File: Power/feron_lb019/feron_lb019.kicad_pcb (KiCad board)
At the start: 2 copper layers, 198 x 53 mm, 51 parts, among them J1 Conn_4pin01, J2 Conn_3pin01, P1 PC817, T1 TF8N60, U2 TL431, U3 OB2268

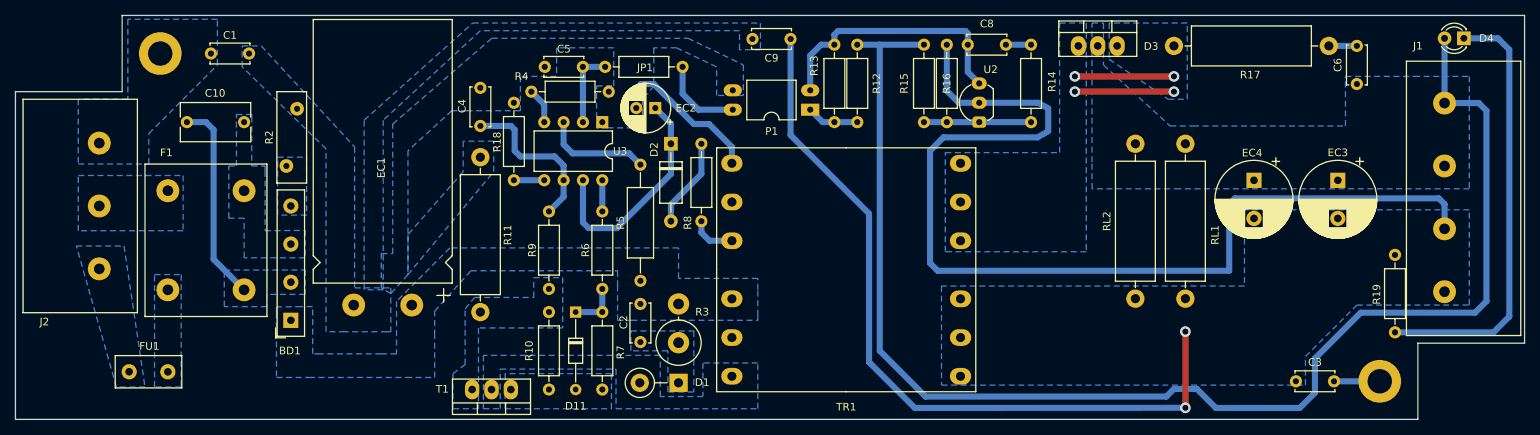
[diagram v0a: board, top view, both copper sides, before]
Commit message: R6. +24V, R1
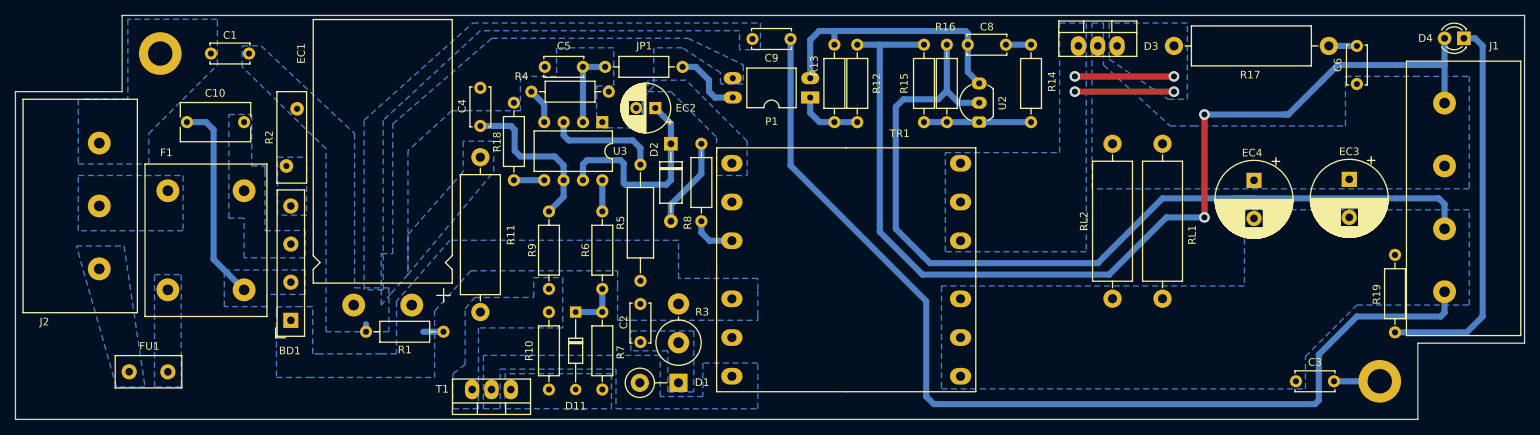
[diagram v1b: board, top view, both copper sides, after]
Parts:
- added R1: 510k, Resistor_THT:R_Axial_DIN0207_L6.3mm_D2.5mm_P10.16mm_Horizontal, F.Cu at (92.2, 111.5)
- RL1, RL2: value 1k -> 2k
- TR1: value Transformer_Feron1 -> PQ3220
- moved RL1 3.00 mm to (186.5, 107.2)
- moved RL2 3.00 mm to (179.9, 107.2)
- moved P1 1.59 mm to (140.3, 80.8)
- moved EC3 1.51 mm to (211.0, 91.5)
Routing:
- net /+24V: track 180.3 -> 137.5 mm, vias 0 -> 2
- net GND1: track 17.6 -> 1.00 mm
- net GND: track 235.6 -> 251.9 mm, vias 2 -> 0
- net Net-(D4-C): track 57.4 -> 50.7 mm
- net /+310V: track 0.00 -> 2.66 mm
- net Net-(D2-C): track 29.8 -> 27.2 mm
- net Net-(P1B-C): track 11.0 -> 9.13 mm
- net Net-(P1A-A): track 6.85 -> 8.68 mm
- net Net-(P1A-C): track 34.8 -> 35.4 mm
- net Net-(U3-VIN): track 14.1 -> 14.7 mm

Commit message: Add L1R20C7
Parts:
- removed RL2: 2k, Resistor_THT:R_Axial_DIN0516_L15.5mm_D5.0mm_P20.32mm_Horizontal
- added C7: NA, Capacitor_THT:C_Disc_D5.0mm_W2.5mm_P5.00mm, F.Cu at (167.5, 85.8)
- added EC5: 1000x35, Capacitor_THT:CP_Radial_D10.0mm_P5.00mm, F.Cu at (213.0, 94.0)
- added L1: LFERR, _aTransformers:dross03, F.Cu at (208.1, 89.7)
- added R20: NA, Resistor_THT:R_Axial_DIN0207_L6.3mm_D2.5mm_P10.16mm_Horizontal, F.Cu at (170.5, 85.8)
- R15: value 33k -> 27k
- R16: value 3k -> 3k3
- moved EC3 9.71 mm to (201.6, 94.0)
- moved EC4 8.63 mm to (190.2, 94.2)
- moved RL1 8.00 mm to (178.5, 107.2)
- moved C6 5.68 mm to (214.7, 74.0), turned to 180 degrees
- moved R14 5.09 mm to (164.5, 85.8)
- moved R15 3.35 mm to (152.0, 85.0)
- moved R16 3.35 mm to (155.0, 74.8)
- moved C8 3.29 mm to (162.8, 73.1)
- moved U2 3.25 mm to (159.4, 85.0)
- moved R17 1.96 mm to (186.0, 74.0)
- moved R19 1.10 mm to (217.0, 102.5)
- moved R12 1.00 mm to (146.4, 85.0)
- moved R13 1.00 mm to (143.4, 74.8)
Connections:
- C6 pad 1: /+24V -> Net-(D3-K)
- D3 pad 2: /+24V -> Net-(D3-K)
- EC3 pad 1: /+24V -> Net-(D3-K)
- EC4 pad 1: /+24V -> Net-(D3-K)
- RL1 pad 2: /+24V -> Net-(D3-K)
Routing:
- net Net-(D3-K): track 0.00 -> 16.5 mm
- net GND: track 251.9 -> 239.9 mm
- net Net-(P1A-C): track 35.4 -> 45.3 mm
- net Net-(C7-Pad2): track 0.00 -> 6.24 mm
- net /+24V: track 137.5 -> 140.1 mm
- net Net-(D3-A1): track 26.0 -> 24.0 mm
- net Net-(U2-REF): track 14.0 -> 15.8 mm
- net Net-(P1A-A): track 8.68 -> 10.1 mm
- net Net-(C8-Pad1): track 3.25 -> 3.94 mm
- added copper zone on B.Cu, net Net-(D3-K)

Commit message: L1 betw R12&R15
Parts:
- removed R20: NA, Resistor_THT:R_Axial_DIN0207_L6.3mm_D2.5mm_P10.16mm_Horizontal
- moved R12 10.2 mm to (146.4, 74.8), turned to -90 degrees
- moved C7 5.83 mm to (167.5, 80.0), turned to -90 degrees
- moved R14 0.83 mm to (164.5, 85.0)
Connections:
- C7 pad 1: Net-(U2-REF) -> Net-(P1A-C)
- C7 pad 2: Net-(C7-Pad2) -> Net-(U2-REF)
- EC5 pad 1: /+24V -> Net-(D3-K)
- R12 pad 2: /+24V -> Net-(D3-K)
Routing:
- net Net-(D3-K): track 16.5 -> 71.2 mm, vias 0 -> 2
- net Net-(P1A-A): track 10.1 -> 17.9 mm
- net Net-(C7-Pad2): track 6.24 -> 0.00 mm
- net Net-(P1A-C): track 45.3 -> 39.9 mm
- net /+24V: track 140.1 -> 137.5 mm
- net GND: track 239.9 -> 241.3 mm
- net Net-(C8-Pad1): track 3.94 -> 3.11 mm

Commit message: L1betwR12R15
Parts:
- R15: value 27k -> 13k
- R16: value 3k3 -> 1k5
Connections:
- EC5 pad 1: Net-(D3-K) -> /+24V
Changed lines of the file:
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@@
 			)
 		)
-		(property "Value" "3k3"
+		(property "Value" "1k5"
 			(at 5.08 2.37 90)
 			(layer "F.Fab")
@@
 			)
 		)
-		(property "Value" "27k"
+		(property "Value" "13k"
 			(at 5.08 2.37 90)
 			(layer "F.Fab")
@@
 			(layers "*.Cu" "*.Mask")
 			(remove_unused_layers no)
-			(net 36 "Net-(D3-K)")
+			(net 8 "/+24V")
 			(pintype "passive")
 		)
